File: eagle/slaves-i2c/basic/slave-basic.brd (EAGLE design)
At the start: 99.1 x 73.7 mm, 20 parts, among them CON3 SPI, IC3 MCP1703CB, J1 RJ12RIGHTANGLE-I2C, J2 RJ12RIGHTANGLE-I2C, U3 ATMEGA328

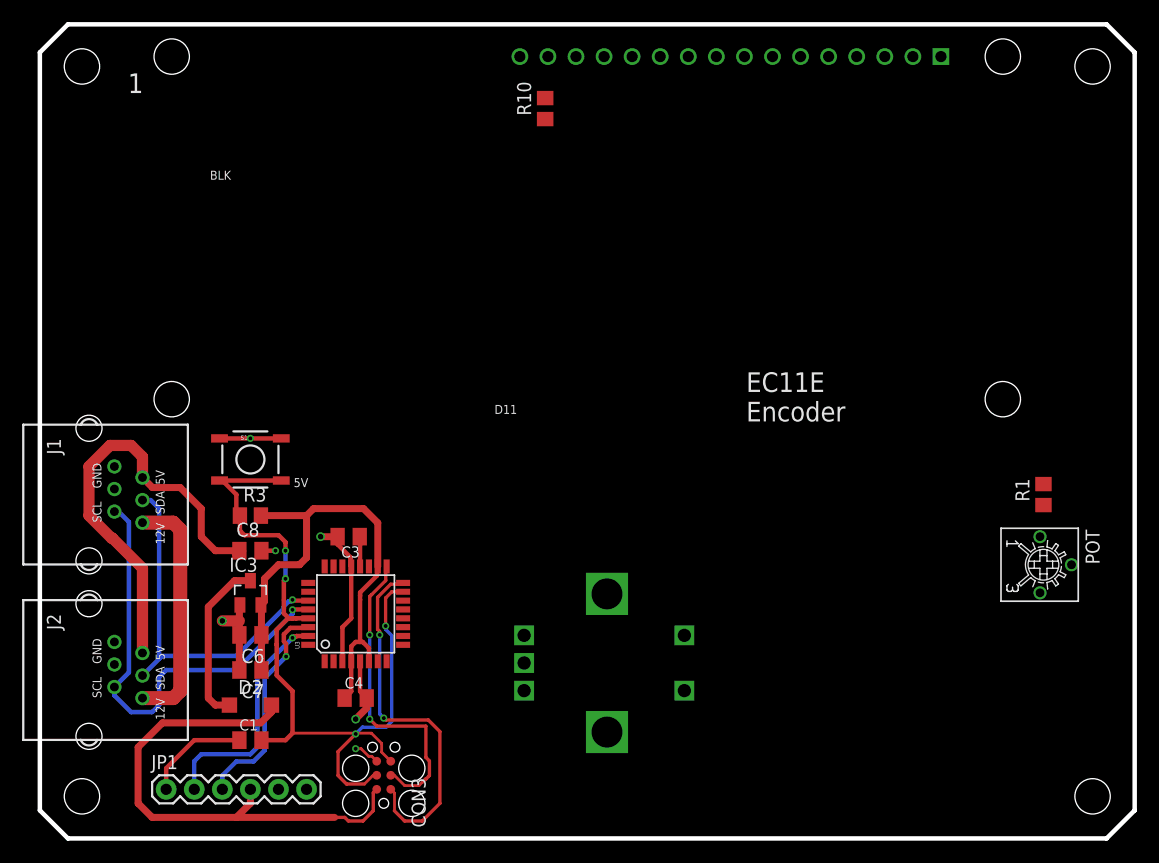
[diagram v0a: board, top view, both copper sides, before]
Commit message: finish slave-basic
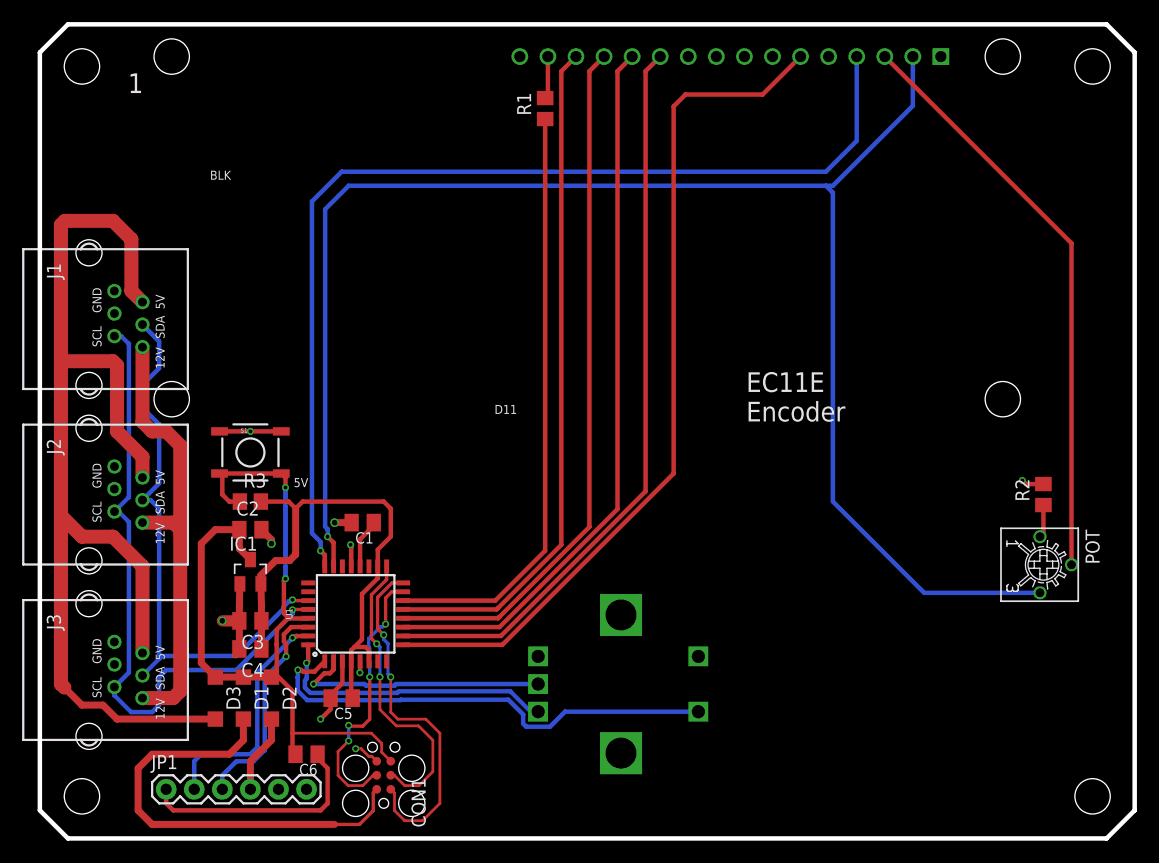
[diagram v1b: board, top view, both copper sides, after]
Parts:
- removed C7: 100nF, rcl:C0805K
- removed C8: 10u, rcl:C0805K
- removed IC3: MCP1703CB, linear:SOT23
- removed R10: 0, rcl:R0805
- removed U3: ATMEGA328, SparkFun:TQFP32-08
- added C2: 10u, rcl:C0805K
- added C5: 100nF, rcl:C0805K
- added D1, D3: Schottky, diode:SOD123
- added IC1: MCP1703CB, linear:SOT23
- added J3: RJ12RIGHTANGLE-I2C, lpatiny:RJ12-RIGHTANGLE-I2C
- added R2: 100, rcl:R0805
- added U1: ATMEGA328P_TQFP, SparkFun-IC-Microcontroller:TQFP32-08
- C3: value 100nF -> 10u
- C6: value 10u -> 100nF
- R1: value 100 -> 0
- moved R1 57.0 mm to (45.7, 66.0)
- moved C1 22.2 mm to (29.2, 28.6), turned to 180 degrees
- moved J1 15.9 mm to (4.45, 47.0)
- moved J2 15.9 mm to (4.45, 31.1)
- moved C6 11.9 mm to (24.1, 7.62)
- moved C3 11.7 mm to (19.1, 19.7)
- moved C4 10.5 mm to (19.1, 17.1), turned to 180 degrees
- moved U$1 2.29 mm to (45.1, 14.0)
- moved D2 2.01 mm to (21.0, 12.7), turned to 270 degrees
- moved R3 1.27 mm to (19.1, 30.5)
- moved S1 0.63 mm to (19.1, 34.9)
- renumbered CON3 to CON1
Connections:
- removed net D13: LCD.2, POT.3, R10.1
- new net +XV: C2.1, D1.C, D2.C, D3.C, IC1.3
- new net EXT-FTDI: D2.A, JP1.4
- net +12V: now also J3.+12V
- net +5V: now also D3.A, J3.+5V; no longer C8.1, D2.C, IC3.3
- net A0: now also LCD.2, POT.3, U1.23; no longer U3.23
- net A1: now also LCD.4, U1.24; no longer U3.24
- net A2: now also U1.25; no longer U3.25
- net A3: now also U1.26; no longer U3.26
- net A6: now also U1.19; no longer LCD.4, U3.19
- net A7: now also U1.22; no longer U3.22
- net AREF: now also C1.1, U1.20; no longer C3.1, U3.20
- net D10: now also R1.1, U1.14; no longer LCD.13, U3.14
- net D2: now also U$1.A, U1.32; no longer U3.32
- net D3: now also U$1.D, U1.1; no longer U3.1
- net D4: now also U$1.B, U1.2; no longer U3.2
- net D5: now also LCD.6, U1.9; no longer LCD.14, U3.9
- net D6: now also LCD.11, U1.10; no longer LCD.6, U3.10
- net D7: now also LCD.12, U1.11; no longer U$1.D, U3.11
- net D8: now also LCD.13, U1.12; no longer LCD.11, U3.12
- net D9: now also LCD.14, U1.13; no longer LCD.12, U3.13
- net DTR: now also C6.1; no longer C1.1
- net EXT-VCC: now also D1.A; no longer D2.A, JP1.4
- net GND: now also C1.2, C2.2, C5.2, IC1.1, J3.GND1, J3.GND2, R2.2, U1.21, U1.3, U1.5; no longer C6.2, C7.2, C8.2, IC3.1, R1.2, U3.21, U3.3, U3.5
- net MISO: now also U1.16; no longer U3.16
- net MOSI: now also U1.15; no longer U3.15
- net N$11: now also R1.2; no longer R10.2
- net N$4: now also R2.1; no longer R1.1
- net RESET: now also C6.2, U1.29; no longer C1.2, U3.29
- net RX: now also U1.30; no longer U$1.B, U3.30
- net SCK: now also U1.17; no longer U3.17
- net SCL: now also J3.SCL, U1.28; no longer U3.28
- net SDA: now also J3.SDA, U1.27; no longer U3.27
- net TX: now also U1.31; no longer U$1.A, U3.31
- net VCC: now also C3.1, C5.1, IC1.2, U1.18, U1.4, U1.6; no longer C6.1, C7.1, IC3.2, U3.18, U3.4, U3.6
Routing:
- net A0: track 0.00 -> 145.1 mm, vias 0 -> 1
- net A1: track 0.00 -> 92.7 mm, vias 0 -> 1
- net D5: track 0.00 -> 77.5 mm
- net D6: track 0.00 -> 67.2 mm
- net D7: track 0.00 -> 65.3 mm
- net D8: track 0.00 -> 63.4 mm
- net D9: track 0.00 -> 61.5 mm
- net D10: track 0.00 -> 53.8 mm
- net N$2: track 0.00 -> 53.0 mm
- net +5V: track 55.2 -> 104.2 mm
- net D3: track 0.00 -> 43.4 mm, vias 0 -> 1
- net D2: track 0.00 -> 26.1 mm, vias 0 -> 1
- net +XV: track 0.00 -> 24.8 mm
- net D4: track 0.00 -> 23.5 mm, vias 0 -> 1
- net +12V: track 22.0 -> 40.6 mm
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
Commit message: add documentation and move lcd-screen
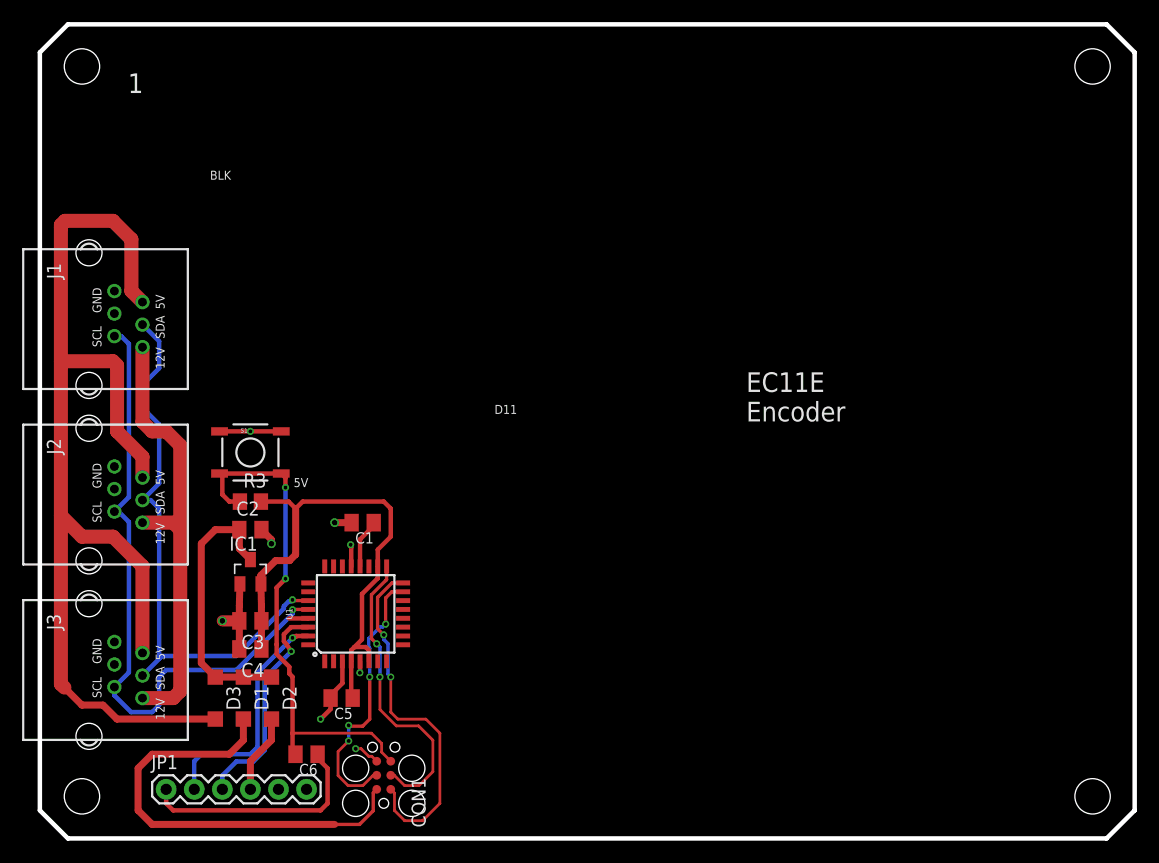
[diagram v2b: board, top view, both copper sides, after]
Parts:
- removed LCD: LCD-HD447804-HOLES16X2-4-HOLES, HD44780LCD:LCD-16X2-4HOLES
- removed POT: 10k, dp_devices:TRIMMER_3362P
- removed R1: 0, rcl:R0805
- removed R2: 100, rcl:R0805
- removed U$1: EC11E, lpatiny:EC11E
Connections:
- removed net N$11: LCD.15, R1.2
- removed net N$2: LCD.3, POT.2
- removed net N$4: POT.1, R2.1
- net A0: no longer LCD.2, POT.3
- net A1: no longer LCD.4
- net D10: no longer R1.1
- net D2: no longer U$1.A
- net D3: no longer U$1.D
- net D4: no longer U$1.B
- net D5: no longer LCD.6
- net D6: no longer LCD.11
- net D7: no longer LCD.12
- net D8: no longer LCD.13
- net D9: no longer LCD.14
- net GND: no longer LCD.1, LCD.16, LCD.5, R2.2, U$1.C, U$1.E
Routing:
- net A0: track 145.1 -> 0.00 mm, vias 1 -> 0
- net A1: track 92.7 -> 0.00 mm, vias 1 -> 0
- net D5: track 77.5 -> 0.00 mm
- net D6: track 67.2 -> 0.00 mm
- net D7: track 65.3 -> 0.00 mm
- net D8: track 63.4 -> 0.00 mm
- net D9: track 61.5 -> 0.00 mm
- net D10: track 53.8 -> 0.00 mm
- net N$2: track 53.0 -> 0.00 mm
- net D3: track 43.4 -> 0.00 mm, vias 1 -> 0
- net D2: track 26.1 -> 0.00 mm, vias 1 -> 0
- net D4: track 23.5 -> 0.00 mm, vias 1 -> 0
- net N$11: track 3.86 -> 0.00 mm
- net N$4: track 2.99 -> 0.00 mm
- net GND: track 29.7 -> 27.7 mm, vias 9 -> 8
